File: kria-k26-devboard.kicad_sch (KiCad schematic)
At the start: 6 parts

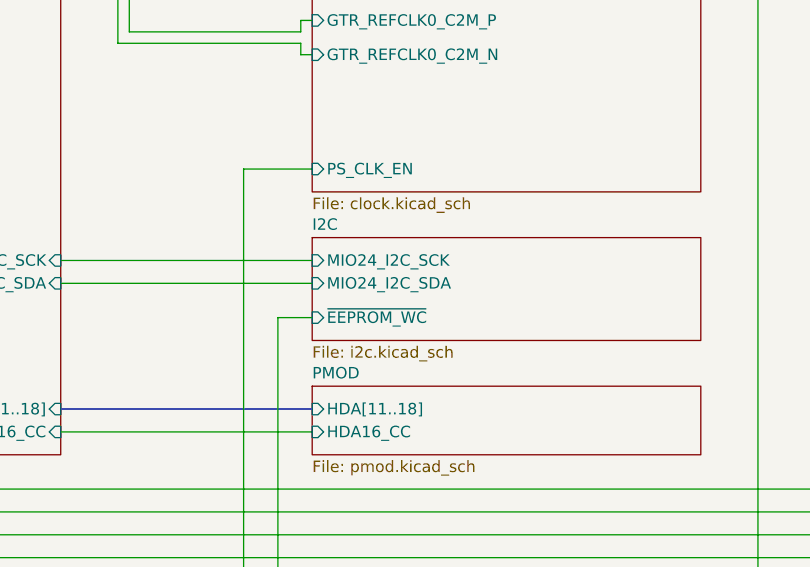
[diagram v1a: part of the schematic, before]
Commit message: Add mandatory pullup to TPS2116 status signal
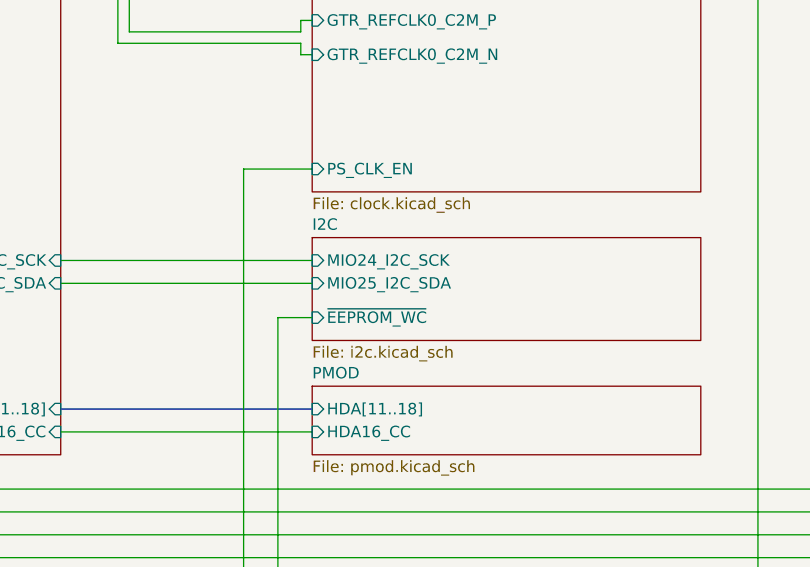
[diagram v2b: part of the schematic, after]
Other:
- sheet I2C  ports: added MIO25_I2C_SDA; removed MIO24_I2C_SDA
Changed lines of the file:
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@@
       (effects (font (size 1.27 1.27)) (justify left))
     )
-    (pin "MIO24_I2C_SDA" input (at 250.19 218.44 180)
+    (pin "~{EEPROM_WC}" input (at 250.19 222.25 180)
       (effects (font (size 1.27 1.27)) (justify left))
     )
-    (pin "~{EEPROM_WC}" input (at 250.19 222.25 180)
+    (pin "MIO25_I2C_SDA" input (at 250.19 218.44 180)
       (effects (font (size 1.27 1.27)) (justify left))
     )
@@
       (reference "R166") (unit 1) (value "R_0R_0402") (footprint "kria-k26-devboard-footprints:0402-res")
     )
+    (path "/00000000-0000-0000-0000-0000630339ce/4fd6095f-7fce-4ff6-b43b-c3e4465fc7ad"
+      (reference "R?") (unit 1) (value "R_10k_0402") (footprint "antmicro-footprints:0402-res")
+    )
     (path "/00000000-0000-0000-0000-000065aaf1bf/00000000-0000-0000-0000-000065caccc2"
       (reference "S1") (unit 1) (value "KMR2") (footprint "kria-k26-devboard-footprints:SW_SPST_4.2x2.8")
@@
       (reference "TP59") (unit 1) (value "TP_SMD_0_75MM") (footprint "kria-k26-devboard-footprints:Testpoint_smd_0_75mm")
     )
+    (path "/00000000-0000-0000-0000-0000630339ce/ccfb62c9-3663-4ef3-918a-99d1f243469c"
+      (reference "TP?") (unit 1) (value "TP_SMD_0_75MM") (footprint "antmicro-footprints:Testpoint_smd_0_75mm")
+    )
     (path "/00000000-0000-0000-0000-000063aa2bfe/d0a380e6-f6c0-4eee-a45e-c7058832611c"
